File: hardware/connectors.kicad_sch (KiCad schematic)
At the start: 27 parts, among them J1 Kenwood-2.5, J10 UART, J11 Radio_Opt, J12 Speaker, J13 KH-RJ45-58-8P8C, J2 USB_C, J301 +12V, J301 OLED, J412 Hirose FH12-22S-0.5SH(55), J413 Molex 532610271, J5 Kenwood-3.5, J7 Radio, J9 STLink, U3 USBLC6-2

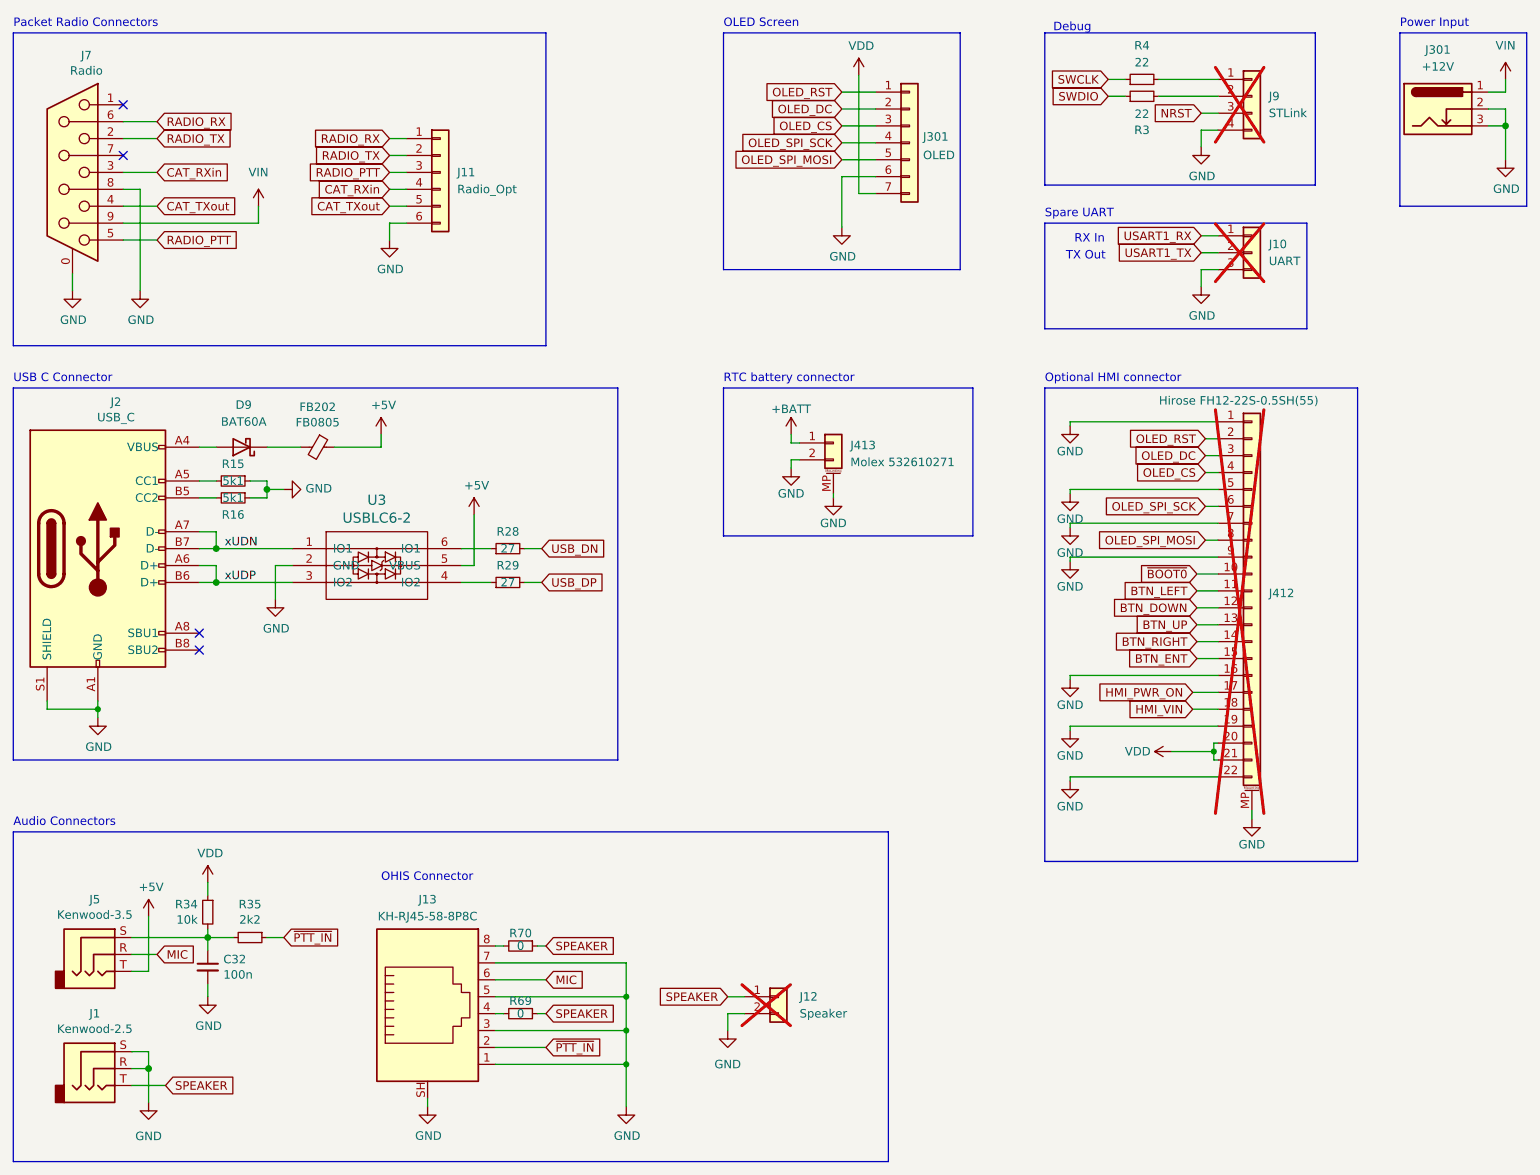
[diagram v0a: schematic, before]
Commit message: Replaced pkl symbols with kicad library symbols
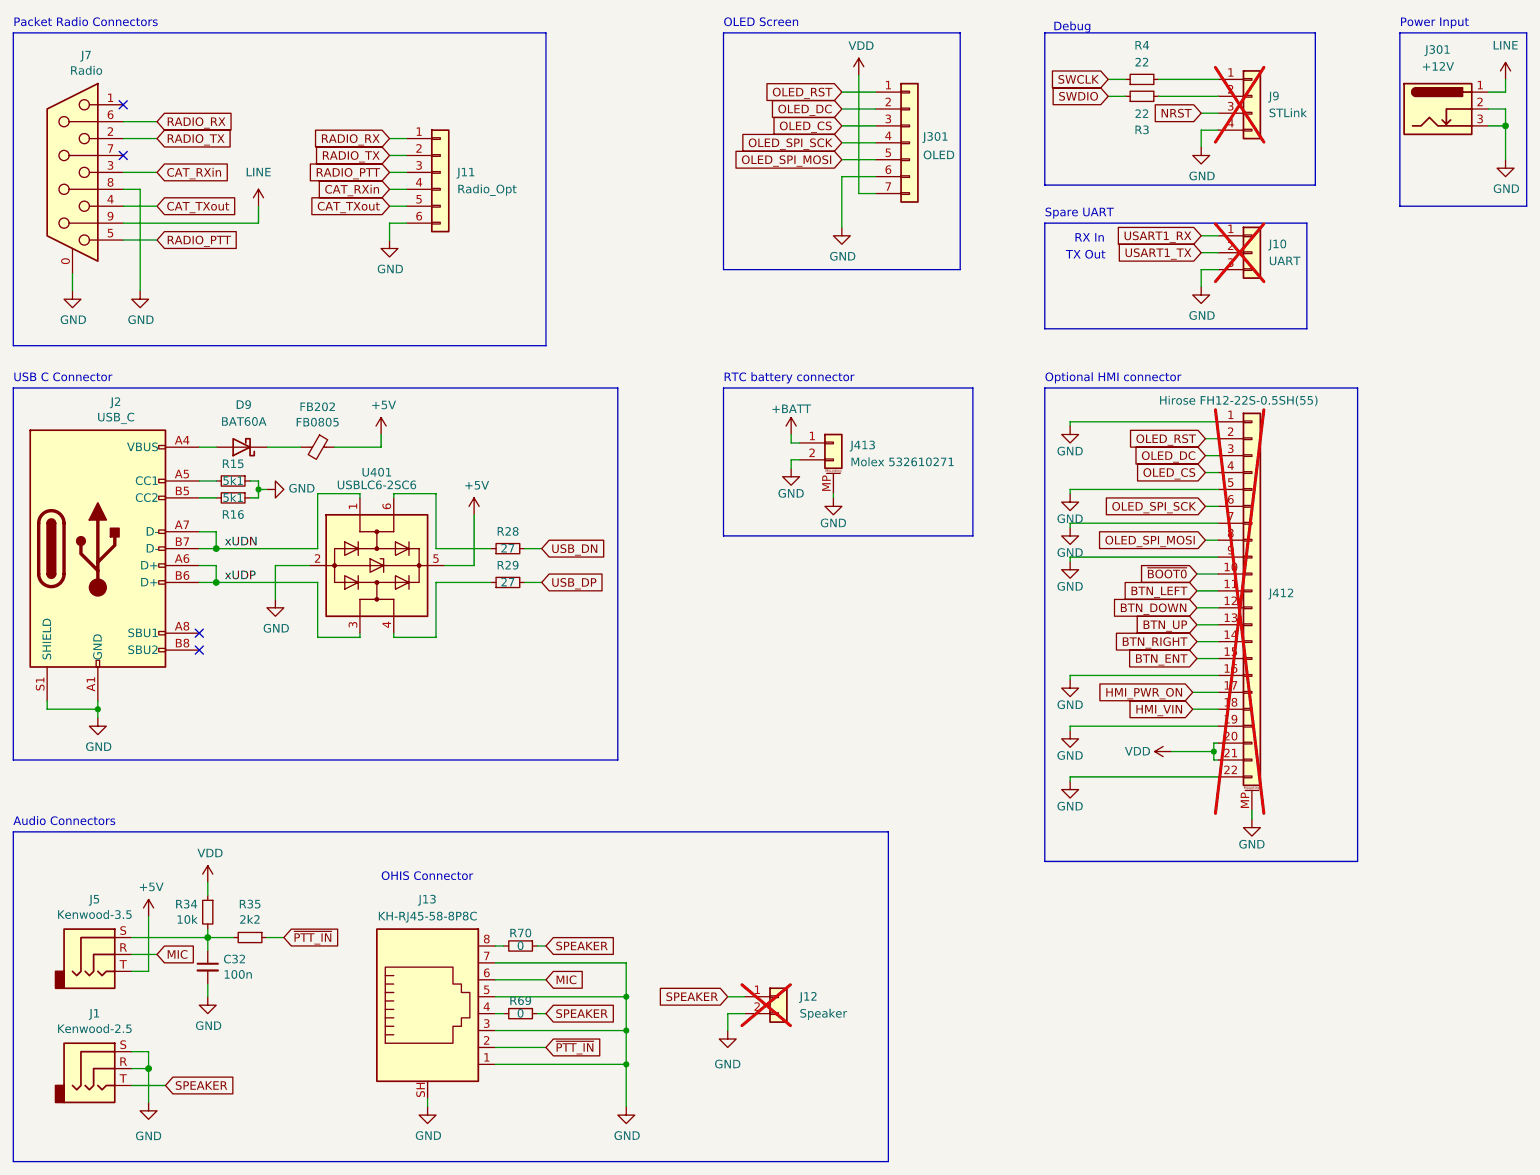
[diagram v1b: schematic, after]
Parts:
- removed U3: USBLC6-2, pkl_housings_sot:SOT-23-6, symbol pkl_misc:USBLC6-2
- added U401: USBLC6-2SC6, pkl_housings_sot:SOT-23-6, symbol Power_Protection:USBLC6-2SC6
- C32: symbol pkl_device:pkl_C_Small -> Device:C_Small
- R15, R16, R28, R29, R3, R34, R35, R4, R69, R70: symbol pkl_device:pkl_R_Small -> Device:R_Small
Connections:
- net +5V: now also U401.5 (VBUS)
- net GND: now also U401.2 (GND)
- net xUDN: now also U401.1 (I/O1)
- net xUDP: now also U401.3 (I/O2)
- net at R28.1: now also U401.6 (I/O1)
- net at R29.1: now also U401.4 (I/O2)
- net VIN renamed LINE

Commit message: Replaced pkl footprints with kicad standard library footprints
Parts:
- C32: footprint pkl_dipol:C_0603 -> Capacitor_SMD:C_0603_1608Metric
- FB202: footprint pkl_dipol:L_0805 -> Inductor_SMD:L_0805_2012Metric
- J2: footprint pkl_connectors:USB_C_Receptacle_HRO_TYPE-C-31-M-12 -> Connector_USB:USB_C_Receptacle_HRO_TYPE-C-31-M-12
- R15, R16, R28, R29, R3, R34, R35, R4, R69, R70: footprint pkl_dipol:R_0603 -> Resistor_SMD:R_0603_1608Metric
- U401: footprint pkl_housings_sot:SOT-23-6 -> Package_TO_SOT_SMD:SOT-23-6
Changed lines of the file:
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@@
       (effects (font (size 1.27 1.27)))
     )
-    (property "Footprint" "pkl_dipol:R_0603" (at 57.15 88.265 0)
+    (property "Footprint" "Resistor_SMD:R_0603_1608Metric" (at 57.15 88.265 0)
       (effects (font (size 1.524 1.524)) hide)
     )
@@
       (effects (font (size 1.27 1.27)) (justify left))
     )
-    (property "Footprint" "pkl_dipol:C_0603" (at 53.34 158.75 0)
+    (property "Footprint" "Capacitor_SMD:C_0603_1608Metric" (at 53.34 158.75 0)
       (effects (font (size 1.524 1.524)) hide)
     )
@@
       (effects (font (size 1.27 1.27)) (justify left))
     )
-    (property "Footprint" "pkl_dipol:R_0603" (at 53.34 150.495 0)
+    (property "Footprint" "Resistor_SMD:R_0603_1608Metric" (at 53.34 150.495 0)
       (effects (font (size 1.524 1.524)) hide)
     )
@@
       (effects (font (size 1.27 1.27)))
     )
-    (property "Footprint" "pkl_dipol:R_0603" (at 100.33 155.575 0)
+    (property "Footprint" "Resistor_SMD:R_0603_1608Metric" (at 100.33 155.575 0)
       (effects (font (size 1.524 1.524)) hide)
     )
@@
       (effects (font (size 1.27 1.27)))
     )
-    (property "Footprint" "pkl_dipol:L_0805" (at 69.85 78.867 90)
+    (property "Footprint" "Inductor_SMD:L_0805_2012Metric" (at 69.85 78.867 90)
       (effects (font (size 1.27 1.27)) hide)
     )
@@
       (effects (font (size 1.27 1.27)))
     )
-    (property "Footprint" "pkl_dipol:R_0603" (at 59.69 154.305 0)
+    (property "Footprint" "Resistor_SMD:R_0603_1608Metric" (at 59.69 154.305 0)
       (effects (font (size 1.524 1.524)) hide)
     )
@@
       (effects (font (size 1.27 1.27)))
     )
-    (property "Footprint" "pkl_dipol:R_0603" (at 98.425 95.885 0)
+    (property "Footprint" "Resistor_SMD:R_0603_1608Metric" (at 98.425 95.885 0)
       (effects (font (size 1.524 1.524)) hide)
     )
@@
       (effects (font (size 1.27 1.27)))
     )
-    (property "Footprint" "pkl_housings_sot:SOT-23-6" (at 66.04 98.425 0)
+    (property "Footprint" "Package_TO_SOT_SMD:SOT-23-6" (at 66.04 98.425 0)
       (effects (font (size 1.27 1.27)) hide)
     )
@@
       (effects (font (size 1.27 1.27)))
     )
-    (property "Footprint" "pkl_dipol:R_0603" (at 98.425 100.965 0)
+    (property "Footprint" "Resistor_SMD:R_0603_1608Metric" (at 98.425 100.965 0)
       (effects (font (size 1.524 1.524)) hide)
     )
@@
       (effects (font (size 1.27 1.27)))
     )
-    (property "Footprint" "pkl_connectors:USB_C_Receptacle_HRO_TYPE-C-31-M-12" (at 40.64 95.885 0)
+    (property "Footprint" "Connector_USB:USB_C_Receptacle_HRO_TYPE-C-31-M-12" (at 40.64 95.885 0)
       (effects (font (size 1.27 1.27)) hide)
     )
@@
       (effects (font (size 1.27 1.27)))
     )
-    (property "Footprint" "pkl_dipol:R_0603" (at 57.15 85.725 0)
+    (property "Footprint" "Resistor_SMD:R_0603_1608Metric" (at 57.15 85.725 0)
       (effects (font (size 1.524 1.524)) hide)
     )
@@
       (effects (font (size 1.27 1.27)))
     )
-    (property "Footprint" "pkl_dipol:R_0603" (at 193.675 25.4 0)
+    (property "Footprint" "Resistor_SMD:R_0603_1608Metric" (at 193.675 25.4 0)
       (effects (font (size 1.524 1.524)) hide)
     )
@@
       (effects (font (size 1.27 1.27)))
     )
-    (property "Footprint" "pkl_dipol:R_0603" (at 193.675 27.94 0)
+    (property "Footprint" "Resistor_SMD:R_0603_1608Metric" (at 193.675 27.94 0)
       (effects (font (size 1.524 1.524)) hide)
     )
@@
       (effects (font (size 1.27 1.27)))
     )
-    (property "Footprint" "pkl_dipol:R_0603" (at 100.33 165.735 0)
+    (property "Footprint" "Resistor_SMD:R_0603_1608Metric" (at 100.33 165.735 0)
       (effects (font (size 1.524 1.524)) hide)
     )

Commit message: Updated title blocks
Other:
- company: (none) -> M17Project
- title: (none) -> Module17
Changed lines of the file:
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@@
 (kicad_sch (version 20230121) (generator eeschema)
   (paper "A4")
+  (title_block
+    (title "Module17")
+    (date "2023-12-06")
+    (rev "Rev 0.99")
+    (company "M17Project")
+    (comment 1 "Morgan ON4MOD")
+    (comment 2 "Mathis - DB9MAT")
+    (comment 3 "Wojciech - SP5WWP")
+  )
   (junction (at 36.83 120.015) (diameter 0) (color 0 0 0 0)
   )

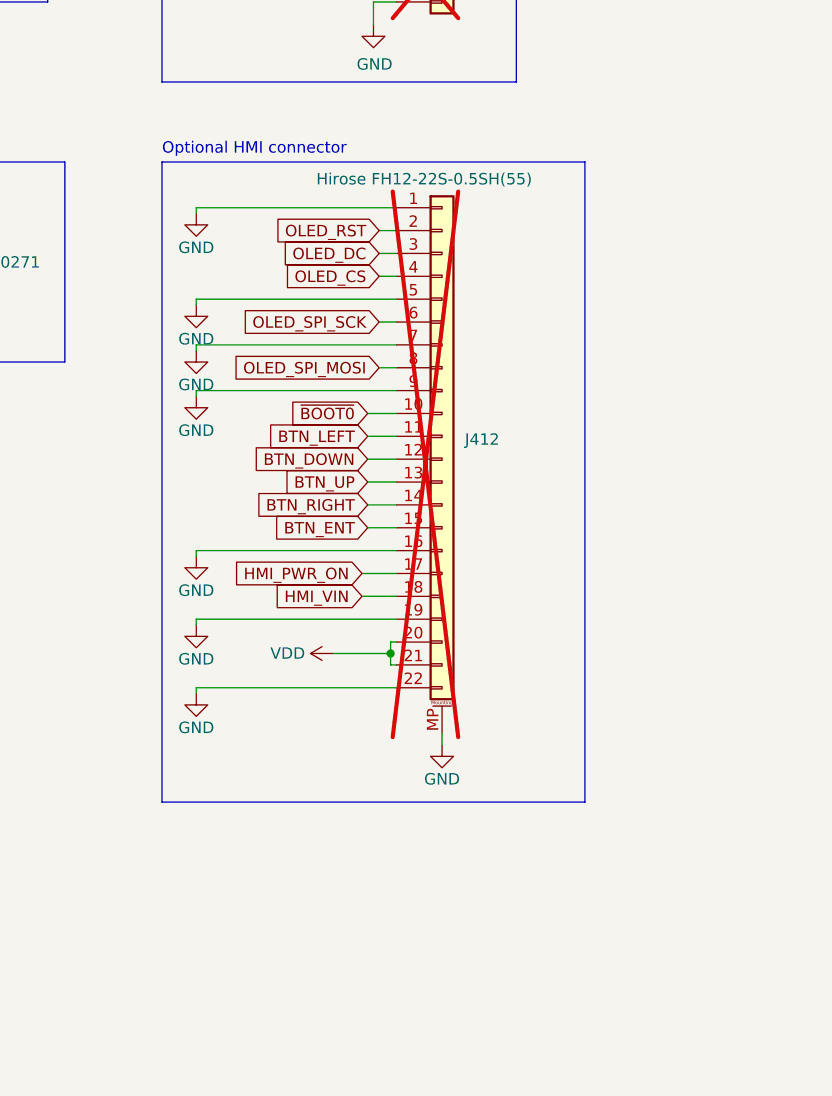
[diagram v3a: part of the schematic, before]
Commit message: Added LEDs signals to HMI connector
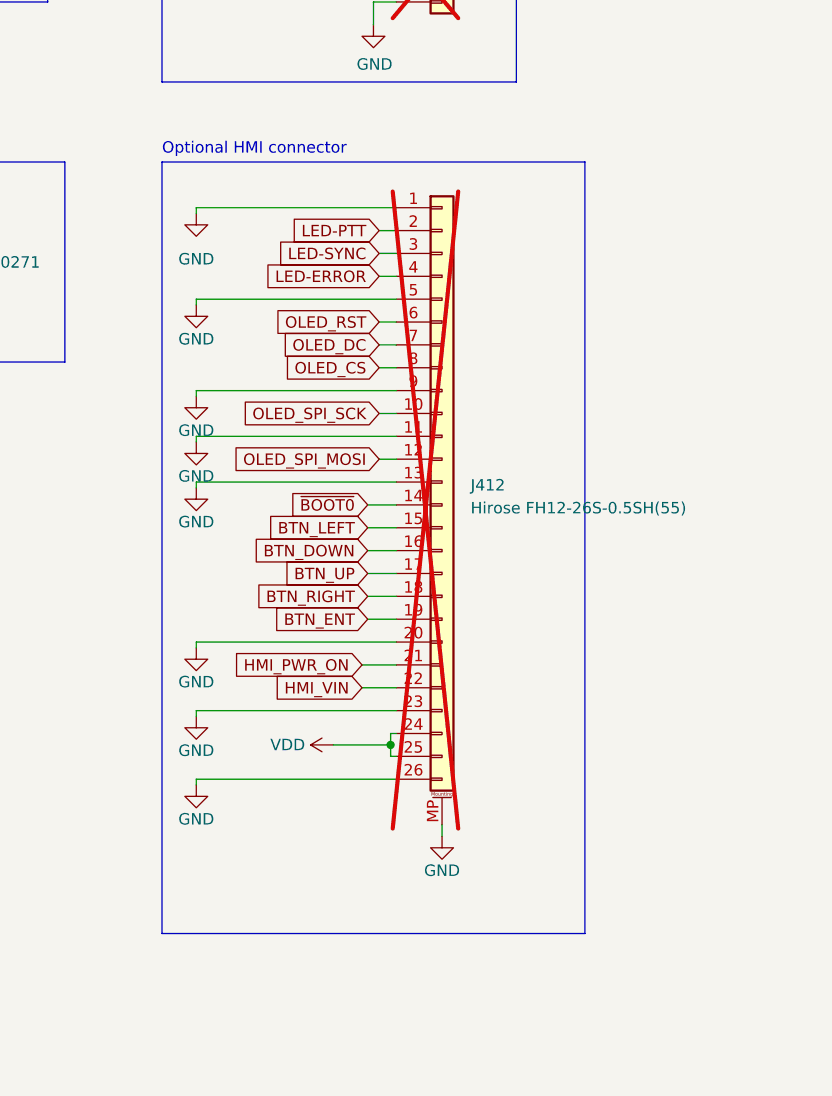
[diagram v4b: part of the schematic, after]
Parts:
- removed J412: Hirose FH12-22S-0.5SH(55), Connector_FFC-FPC:Hirose_FH12-22S-0.5SH_1x22-1MP_P0.50mm_Horizontal, symbol Connector_Generic_MountingPin:Conn_01x22_MountingPin
- added J412: Hirose FH12-26S-0.5SH(55), Connector_FFC-FPC:Hirose_FH12-26S-0.5SH_1x26-1MP_P0.50mm_Horizontal, symbol Connector_Generic_MountingPin:Conn_01x26_MountingPin
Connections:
- net BTN_DOWN: now also J412.16 (Pin_16)
- net BTN_ENT: now also J412.19 (Pin_19)
- net BTN_LEFT: now also J412.15 (Pin_15)
- net BTN_RIGHT: now also J412.18 (Pin_18)
- net BTN_UP: now also J412.17 (Pin_17)
- net GND: now also J412.1 (Pin_1), J412.11 (Pin_11), J412.13 (Pin_13), J412.20 (Pin_20), J412.23 (Pin_23), J412.26 (Pin_26), J412.5 (Pin_5), J412.9 (Pin_9), J412.MP (MountPin)
- net HMI_PWR_ON: now also J412.21 (Pin_21)
- net HMI_VIN: now also J412.22 (Pin_22)
- net OLED_CS: now also J412.8 (Pin_8)
- net OLED_DC: now also J412.7 (Pin_7)
- net OLED_RST: now also J412.6 (Pin_6)
- net OLED_SPI_MOSI: now also J412.12 (Pin_12)
- net OLED_SPI_SCK: now also J412.10 (Pin_10)
- net VDD: now also J412.24 (Pin_24), J412.25 (Pin_25)
- net ~{BOOT0}: now also J412.14 (Pin_14)
- new net LED-ERROR: J412.4 (Pin_4)
- new net LED-PTT: J412.2 (Pin_2)
- new net LED-SYNC: J412.3 (Pin_3)
